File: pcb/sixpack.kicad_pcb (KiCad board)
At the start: 2 copper layers, 28 parts, among them SW1 SW_Push, U1 ATmega32U4-AU, Y1 16MHz

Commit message: finished routing
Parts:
- moved R3 121.8 mm to (108.2, 53.3)
- moved C5 117.1 mm to (111.7, 53.1), turned to 90 degrees
- moved Y1 116.9 mm to (115.1, 53.1), turned to 180 degrees
- moved C3 116.1 mm to (114.2, 56.0), turned to 180 degrees
- moved D2 112.1 mm to (84.0, 50.6), turned to 180 degrees
- moved C1 111.2 mm to (121.9, 64.8), turned to 90 degrees
- moved R4 105.6 mm to (122.7, 70.4)
- moved SW1 104.6 mm to (98.4, 64.5), turned to 180 degrees
- moved C4 103.4 mm to (109.2, 56.1), turned to 0 degrees
- moved D4 103.2 mm to (102.0, 51.7), turned to 270 degrees
- moved D3 102.0 mm to (108.0, 83.0)
- moved D1 102.0 mm to (89.0, 83.0)
- moved D5 102.0 mm to (127.0, 83.0)
- moved USB1 101.9 mm to (92.7, 50.1)
- moved U1 101.2 mm to (111.9, 67.0), turned to 0 degrees
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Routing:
- net GND: track 0.00 -> 149.7 mm, vias 0 -> 4
- net +5V: track 0.00 -> 134.0 mm, vias 0 -> 10
- net COL0: track 0.00 -> 101.1 mm, vias 0 -> 1
- net COL1: track 0.00 -> 94.3 mm, vias 0 -> 1
- net ROW0: track 0.00 -> 74.0 mm
- net COL2: track 0.00 -> 70.0 mm, vias 0 -> 1
- net ROW1: track 0.00 -> 65.0 mm
- net Net-(R1-Pad1): track 0.00 -> 23.1 mm
- net Net-(R2-Pad1): track 0.00 -> 21.8 mm
- net Net-(R3-Pad2): track 0.00 -> 17.7 mm
- net Net-(C5-Pad1): track 0.00 -> 10.8 mm
- net Net-(D1-Pad2): track 0.00 -> 9.70 mm
- net Net-(D3-Pad2): track 0.00 -> 9.67 mm
- net VCC: track 0.00 -> 9.30 mm
- net Net-(D5-Pad2): track 0.00 -> 9.11 mm
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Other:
- board outline added: 59.7 x 40.6 mm
- net class Default: trace_width 0.25 -> 0.254
- net class Power added: clearance 0.2, trace_width 0.381, via_dia 0.8, via_drill 0.4

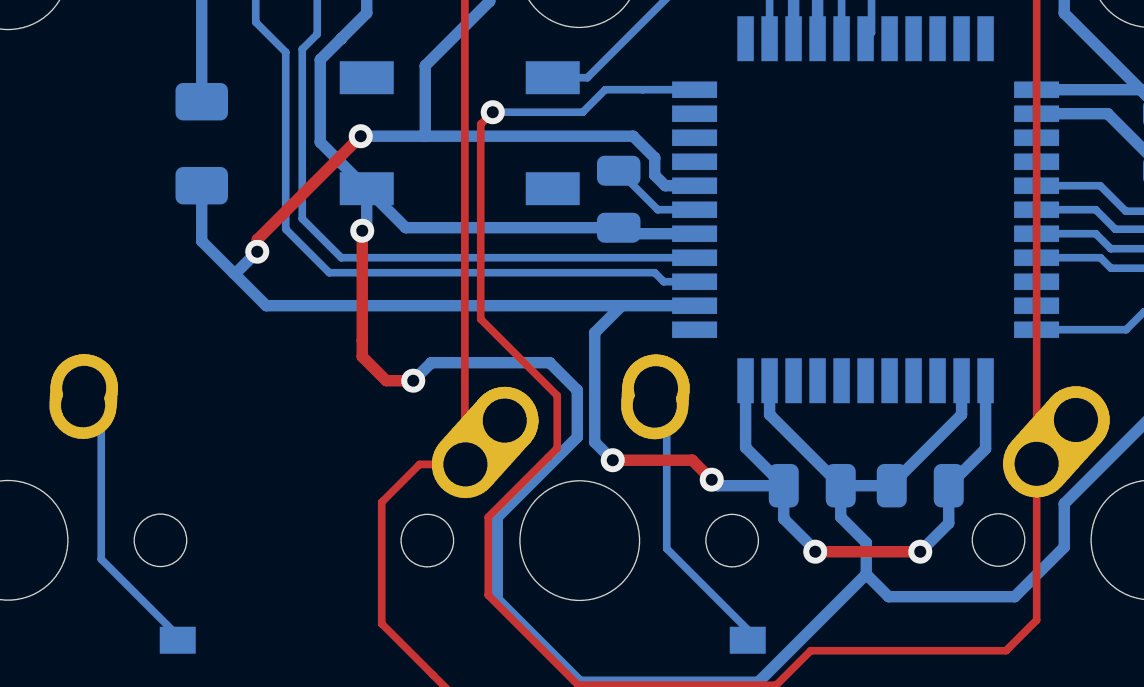
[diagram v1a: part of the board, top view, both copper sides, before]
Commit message: moved 10uF to after the polyfuse
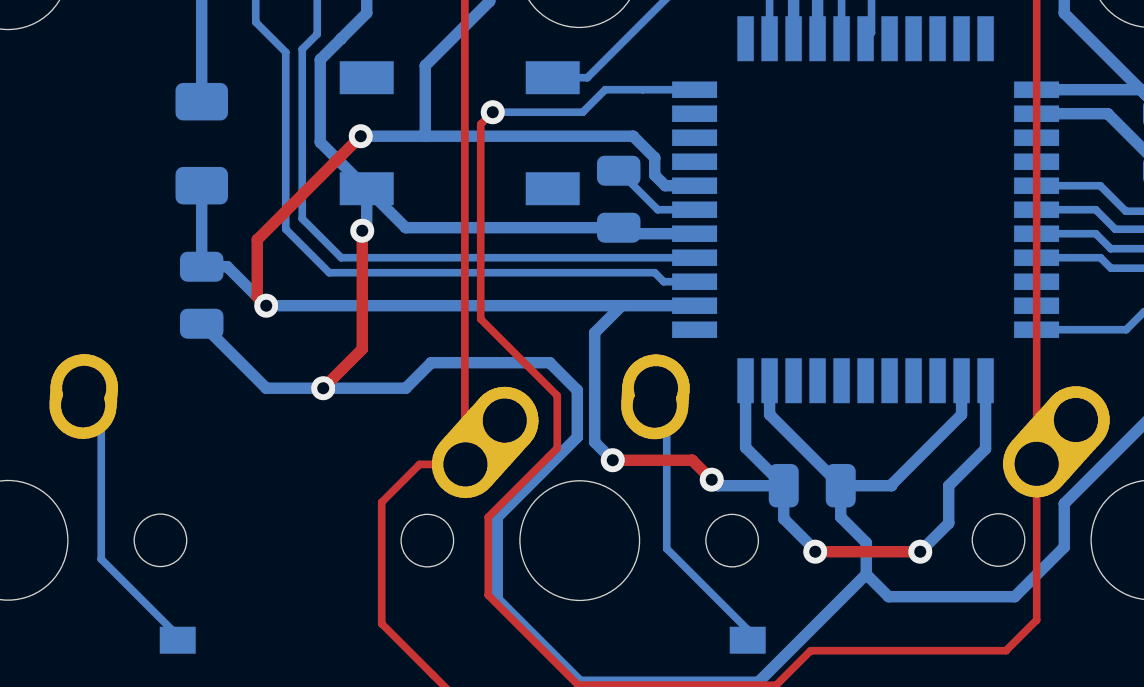
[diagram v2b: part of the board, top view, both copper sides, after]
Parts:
- moved C7 24.8 mm to (89.8, 69.8), turned to 270 degrees
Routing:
- net GND: track 149.7 -> 157.3 mm
- net +5V: track 134.0 -> 135.3 mm
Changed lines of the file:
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@@
     (38 B.Mask user)
     (39 F.Mask user)
-    (40 Dwgs.User user)
+    (40 Dwgs.User user hide)
     (41 Cmts.User user)
     (42 Eco1.User user)
@@
   )
   (module Capacitor_SMD:C_0805_2012Metric (layer B.Cu)
-    (at 113.75 76.2 180)
+    (at 89.8 69.85 270)
     (descr "Capacitor SMD 0805 (2012 Metric), square (rectangular) end terminal, IPC_7351 nominal, (Body size source: IPC-SM-782 page 76, https://www.pcb-3d.com/wordpress/wp-content/uploads/ipc-sm-782a_amendment_1_and_2.pdf, https://docs.google.com/spreadsheets/d/1BsfQQcO9C6DZCsRaXUlFlo91Tg2WpOkGARC1WS5S8t0/edit?usp=sharing), generated with kicad-footprint-generator")
     (tags capacitor)
     (attr smd)
-    (fp_text reference C7 (at 0 1.68) (layer B.SilkS)
-      (effects (font (size 1 1) (thickness 0.15)) (justify mirror))
-    )
-    (fp_text value 10uF (at 0 -1.68) (layer B.Fab)
+    (fp_text reference C7 (at 0 1.68 90) (layer B.SilkS)
+      (effects (font (size 1 1) (thickness 0.15)) (justify mirror))
+    )
+    (fp_text value 10uF (at 0 -1.68 90) (layer B.Fab)
       (effects (font (size 1 1) (thickness 0.15)) (justify mirror))
     )
@@
     (fp_line (start 1.7 0.98) (end 1.7 -0.98) (layer B.CrtYd) (width 0.05))
     (fp_line (start 1.7 -0.98) (end -1.7 -0.98) (layer B.CrtYd) (width 0.05))
-    (fp_text user %R (at 0 0) (layer B.Fab)
+    (fp_text user %R (at 0 0 90) (layer B.Fab)
       (effects (font (size 0.5 0.5) (thickness 0.08)) (justify mirror))
     )
-    (pad 2 smd roundrect (at 0.95 0 180) (size 1 1.45) (layers B.Cu B.Paste B.Mask) (roundrect_rratio 0.25)
-      (net 1 GND))
-    (pad 1 smd roundrect (at -0.95 0 180) (size 1 1.45) (layers B.Cu B.Paste B.Mask) (roundrect_rratio 0.25)
+    (pad 2 smd roundrect (at 0.95 0 270) (size 1 1.45) (layers B.Cu B.Paste B.Mask) (roundrect_rratio 0.25)
+      (net 1 GND))
+    (pad 1 smd roundrect (at -0.95 0 270) (size 1 1.45) (layers B.Cu B.Paste B.Mask) (roundrect_rratio 0.25)
       (net 2 +5V))
     (model ${KISYS3DMOD}/Capacitor_SMD.3dshapes/C_0805_2012Metric.wrl
@@
   (segment (start 95.3 66.3) (end 95.3 67.55) (width 0.381) (layer B.Cu) (net 1))
   (segment (start 95.3 67.55) (end 95.15 67.7) (width 0.381) (layer B.Cu) (net 1))
-  (segment (start 95.15 67.7) (end 95.15 71.35) (width 0.381) (layer F.Cu) (net 1))
   (segment (start 111.1 76.2) (end 111.1 77.25) (width 0.381) (layer B.Cu) (net 1))
   (segment (start 111.1 77.25) (end 111.95 78.1) (width 0.381) (layer B.Cu) (net 1))
-  (segment (start 95.15 71.35) (end 95.15 71.9) (width 0.381) (layer F.Cu) (net 1))
-  (via (at 96.85 72.7) (size 0.8) (drill 0.4) (layers F.Cu B.Cu) (net 1))
-  (segment (start 95.15 71.9) (end 95.95 72.7) (width 0.381) (layer F.Cu) (net 1))
-  (segment (start 95.95 72.7) (end 96.85 72.7) (width 0.381) (layer F.Cu) (net 1))
-  (segment (start 96.85 72.7) (end 97.45 72.1) (width 0.381) (layer B.Cu) (net 1))
   (segment (start 102.31899 74.582096) (end 99.65 77.251086) (width 0.381) (layer B.Cu) (net 1))
   (segment (start 102.31899 73.01899) (end 102.31899 74.582096) (width 0.381) (layer B.Cu) (net 1))
@@
   (segment (start 122.1 71.925) (end 123.625 70.4) (width 0.381) (layer B.Cu) (net 1))
   (segment (start 122.1 73.25) (end 122.1 71.925) (width 0.381) (layer B.Cu) (net 1))
+  (segment (start 89.8 70.8) (end 91.95 72.95) (width 0.381) (layer B.Cu) (net 1))
+  (segment (start 96.6 72.95) (end 97.45 72.1) (width 0.381) (layer B.Cu) (net 1))
+  (segment (start 95.15 67.7) (end 95.15 71.65) (width 0.381) (layer F.Cu) (net 1))
+  (via (at 93.85 72.95) (size 0.8) (drill 0.4) (layers F.Cu B.Cu) (net 1))
+  (segment (start 91.95 72.95) (end 93.85 72.95) (width 0.381) (layer B.Cu) (net 1))
+  (segment (start 95.15 71.65) (end 93.85 72.95) (width 0.381) (layer F.Cu) (net 1))
+  (segment (start 93.85 72.95) (end 96.6 72.95) (width 0.381) (layer B.Cu) (net 1))
   (segment (start 120 63.8) (end 117.628 63.8) (width 0.381) (layer B.Cu) (net 2))
   (segment (start 121.9 65.7) (end 120 63.8) (width 0.381) (layer B.Cu) (net 2))
@@
   (segment (start 108.25 54.2125) (end 109.1625 53.3) (width 0.381) (layer B.Cu) (net 2))
   (segment (start 108.25 56.15) (end 108.25 54.2125) (width 0.381) (layer B.Cu) (net 2))
-  (segment (start 89.8 66.2) (end 89.8 68.05) (width 0.381) (layer B.Cu) (net 2))
   (segment (start 109.1625 53.3) (end 109.1625 51.4875) (width 0.381) (layer B.Cu) (net 2))
   (via (at 109.35 51.3) (size 0.8) (drill 0.4) (layers F.Cu B.Cu) (net 2))
@@
   (segment (start 104.9 65.85) (end 104.9 65.26918) (width 0.381) (layer B.Cu) (net 2))
   (segment (start 104.9 65.26918) (end 104.18082 64.55) (width 0.381) (layer B.Cu) (net 2))
-  (via (at 91.65 68.4) (size 0.8) (drill 0.4) (layers F.Cu B.Cu) (net 2))
   (segment (start 95.1 64.55) (end 91.65 68) (width 0.381) (layer F.Cu) (net 2))
-  (segment (start 91.65 68) (end 91.65 68.4) (width 0.381) (layer F.Cu) (net 2))
-  (segment (start 91.65 68.4) (end 90.925 69.125) (width 0.381) (layer B.Cu) (net 2))
-  (segment (start 90.925 69.125) (end 90.875 69.125) (width 0.381) (layer B.Cu) (net 2))
-  (segment (start 89.8 68.05) (end 90.875 69.125) (width 0.381) (layer B.Cu) (net 2))
-  (segment (start 90.875 69.125) (end 91.95 70.2) (width 0.381) (layer B.Cu) (net 2))
   (segment (start 97.25 64.55) (end 97.25 62.2) (width 0.381) (layer B.Cu) (net 2))
   (segment (start 97.25 64.55) (end 95.1 64.55) (width 0.381) (layer B.Cu) (net 2))
@@
   (segment (start 109.528 61.3) (end 109.528 59.028) (width 0.381) (layer B.Cu) (net 2))
   (segment (start 109.528 59.028) (end 109.528 57.428) (width 0.381) (layer B.Cu) (net 2))
+  (segment (start 89.8 66.2) (end 89.8 68.9) (width 0.381) (layer B.Cu) (net 2))
+  (via (at 91.95 70.2) (size 0.8) (drill 0.4) (layers F.Cu B.Cu) (net 2))
+  (segment (start 89.8 68.9) (end 90.65 68.9) (width 0.381) (layer B.Cu) (net 2))
+  (segment (start 90.65 68.9) (end 91.95 70.2) (width 0.381) (layer B.Cu) (net 2))
+  (segment (start 91.65 69.9) (end 91.95 70.2) (width 0.381) (layer F.Cu) (net 2))
+  (segment (start 91.65 68) (end 91.65 69.9) (width 0.381) (layer F.Cu) (net 2))
   (segment (start 112.125999 61.102001) (end 111.928 61.3) (width 0.254) (layer B.Cu) (net 3))
   (segment (start 112.125999 59.024001) (end 112.125999 61.102001) (width 0.254) (layer B.Cu) (net 3))

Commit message: connected usb ground pads and shrunk gnd plane
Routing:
- net GND: track 157.3 -> 176.1 mm
- net D+: track 0.00 -> 3.25 mm
- net D-: track 0.00 -> 2.99 mm
- added copper zone on B.Cu, net GND
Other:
- board text added: "RyNo~SixPack"

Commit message: Moved labels
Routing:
- net +5V: track 135.3 -> 132.9 mm, vias 10 -> 8
- net Net-(R3-Pad2): track 17.7 -> 19.3 mm, vias 0 -> 2
